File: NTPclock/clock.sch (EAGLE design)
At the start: 20 parts, among them IC1 MAX7219CNG

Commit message: Initial board layout
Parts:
- added R3: 10KΩ, SparkFun-Resistors:RESISTOR1206
- C6: device SparkFun-Capacitors:CAP_POLPTH4 -> SparkFun-Capacitors:CAP_POLPTH1
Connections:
- net +5V renamed VCC
- removed net +3.3V: C5.1, J1.2
- new net 3.3V: C5.1, J1.2, R3.1, U$1.3V3@0, U$1.3V3@1, U$1.3V3@2
- net SQL: now also R3.2
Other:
- moved on the sheet: C1, C2, C3, C4, C5, C6, C7, C8, DOUT, U$1

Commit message: Board update
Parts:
- C6: value (none) -> 470μF
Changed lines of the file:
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@@
 <part name="C4" library="SparkFun-Capacitors" deviceset="CAP" device="1206"/>
 <part name="C5" library="SparkFun-Capacitors" deviceset="CAP" device="1206"/>
-<part name="C6" library="SparkFun-Capacitors" deviceset="CAP_POL" device="PTH1"/>
+<part name="C6" library="SparkFun-Capacitors" deviceset="CAP_POL" device="PTH1" value="470μF"/>
 <part name="C7" library="SparkFun-Capacitors" deviceset="CAP_POL" device="PTH1"/>
 <part name="C8" library="SparkFun-Capacitors" deviceset="CAP_POL" device="PTH1" value="10μF"/>

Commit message: Update Schematic.  (Also break it)
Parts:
- U$1: value ESP12E_DEVKIT -> NODEMCU V3
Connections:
- net CLK: now also U$1.D7; no longer U$1.D6
- net DIGIT0: no longer DIG_3.G1, DIG_3.G2
- net DIGIT1: now also DIG_1.G1, DIG_1.G2; no longer DIG_2.G1, DIG_2.G2
- net DIGIT2: no longer DIG_1.G1, DIG_1.G2
- net DIGIT4: now also DIG_2.G1, DIG_2.G2
- net DIGIT5: now also DIG_3.G1, DIG_3.G2
- net LOAD: now also U$1.D6; no longer U$1.D7
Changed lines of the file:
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@@
 </classes>
 <parts>
-<part name="U$1" library="NODEMCUv1" deviceset="ESP12E_DEVKIT" device=""/>
+<part name="U$1" library="NODEMCUv1" deviceset="ESP12E_DEVKIT" device="" value="NODEMCU V3"/>
 <part name="IC1" library="max7219" deviceset="MAX7219CNG" device=""/>
 <part name="R1" library="SparkFun-Resistors" deviceset="RESISTOR" device="1206"/>
@@
 <net name="DIGIT0" class="0">
 <segment>
-<pinref part="DIG_3" gate="G$1" pin="G1"/>
-<pinref part="DIG_3" gate="G$1" pin="G2"/>
-<wire x1="76.2" y1="17.78" x2="76.2" y2="15.24" width="0.1524" layer="91"/>
-<wire x1="76.2" y1="10.16" x2="76.2" y2="15.24" width="0.1524" layer="91"/>
-<junction x="76.2" y="15.24"/>
-</segment>
-<segment>
 <pinref part="IC1" gate="G$1" pin="DIG0"/>
 <wire x1="58.42" y1="58.42" x2="55.88" y2="58.42" width="0.1524" layer="91"/>
@@
 <net name="DIGIT1" class="0">
 <segment>
-<pinref part="DIG_2" gate="G$1" pin="G1"/>
-<pinref part="DIG_2" gate="G$1" pin="G2"/>
-<wire x1="111.76" y1="17.78" x2="111.76" y2="15.24" width="0.1524" layer="91"/>
-<wire x1="111.76" y1="10.16" x2="111.76" y2="15.24" width="0.1524" layer="91"/>
-<junction x="111.76" y="15.24"/>
-</segment>
-<segment>
 <pinref part="IC1" gate="G$1" pin="DIG1"/>
 <wire x1="58.42" y1="55.88" x2="55.88" y2="55.88" width="0.1524" layer="91"/>
 </segment>
-</net>
-<net name="DIGIT2" class="0">
 <segment>
 <pinref part="DIG_1" gate="G$1" pin="G1"/>
@@
 <junction x="147.32" y="15.24"/>
 </segment>
+</net>
+<net name="DIGIT2" class="0">
 <segment>
 <pinref part="IC1" gate="G$1" pin="DIG2"/>
@@
 <junction x="236.22" y="15.24"/>
 </segment>
+<segment>
+<pinref part="DIG_3" gate="G$1" pin="G1"/>
+<pinref part="DIG_3" gate="G$1" pin="G2"/>
+<wire x1="76.2" y1="17.78" x2="76.2" y2="15.24" width="0.1524" layer="91"/>
+<wire x1="76.2" y1="10.16" x2="76.2" y2="15.24" width="0.1524" layer="91"/>
+<junction x="76.2" y="15.24"/>
+</segment>
 </net>
 <net name="DIGIT4" class="0">
@@
 <junction x="233.68" y="30.48"/>
 </segment>
+<segment>
+<pinref part="DIG_2" gate="G$1" pin="G1"/>
+<pinref part="DIG_2" gate="G$1" pin="G2"/>
+<wire x1="111.76" y1="17.78" x2="111.76" y2="15.24" width="0.1524" layer="91"/>
+</segment>
 </net>
 <net name="DATA" class="0">
@@
 <net name="CLK" class="0">
 <segment>
+<pinref part="IC1" gate="G$1" pin="CLK"/>
+<wire x1="27.94" y1="58.42" x2="20.32" y2="58.42" width="0.1524" layer="91"/>
+<label x="20.32" y="58.42" size="1.778" layer="95"/>
+</segment>
+<segment>
+<pinref part="U$1" gate="G$1" pin="D7"/>
+<wire x1="73.66" y1="101.6" x2="81.28" y2="101.6" width="0.1524" layer="91"/>
+<label x="76.2" y="101.6" size="1.778" layer="95"/>
+</segment>
+</net>
+<net name="LOAD" class="0">
+<segment>
+<pinref part="IC1" gate="G$1" pin="LOAD"/>
+<wire x1="27.94" y1="53.34" x2="20.32" y2="53.34" width="0.1524" layer="91"/>
+<label x="20.32" y="53.34" size="1.778" layer="95"/>
+</segment>
+<segment>
 <pinref part="U$1" gate="G$1" pin="D6"/>
 <wire x1="73.66" y1="104.14" x2="81.28" y2="104.14" width="0.1524" layer="91"/>
 <label x="76.2" y="104.14" size="1.778" layer="95"/>
 </segment>
-<segment>
-<pinref part="IC1" gate="G$1" pin="CLK"/>
-<wire x1="27.94" y1="58.42" x2="20.32" y2="58.42" width="0.1524" layer="91"/>
-<label x="20.32" y="58.42" size="1.778" layer="95"/>
-</segment>
-</net>
-<net name="LOAD" class="0">
-<segment>
-<pinref part="U$1" gate="G$1" pin="D7"/>
-<wire x1="73.66" y1="101.6" x2="81.28" y2="101.6" width="0.1524" layer="91"/>
-<label x="76.2" y="101.6" size="1.778" layer="95"/>
-</segment>
-<segment>
-<pinref part="IC1" gate="G$1" pin="LOAD"/>
-<wire x1="27.94" y1="53.34" x2="20.32" y2="53.34" width="0.1524" layer="91"/>
-<label x="20.32" y="53.34" size="1.778" layer="95"/>
-</segment>
-</net>
+</net>

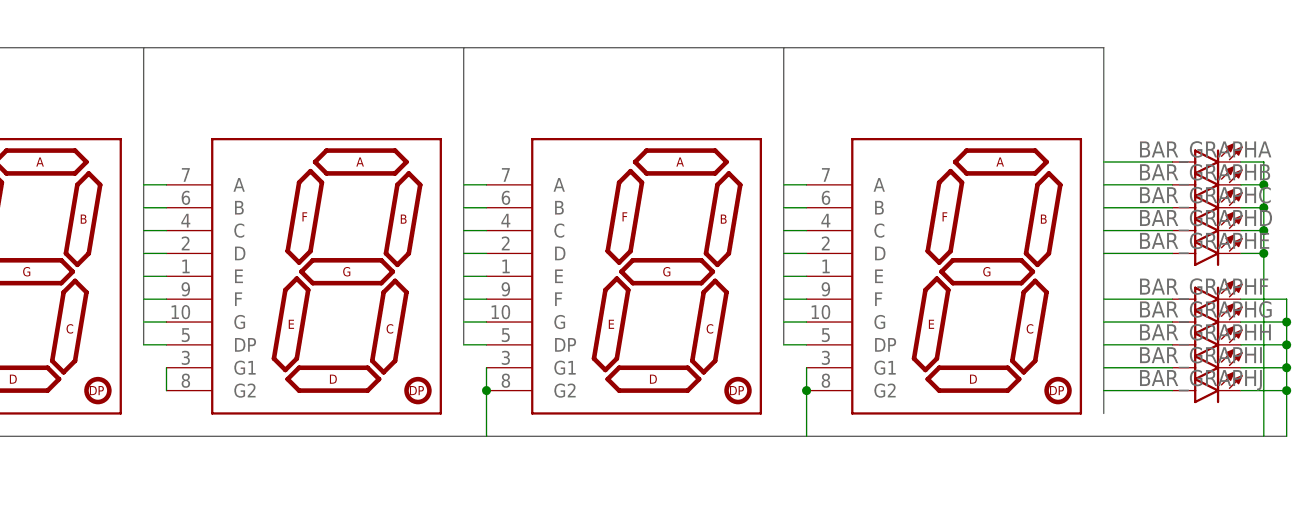
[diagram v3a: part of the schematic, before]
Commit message: rearange digits
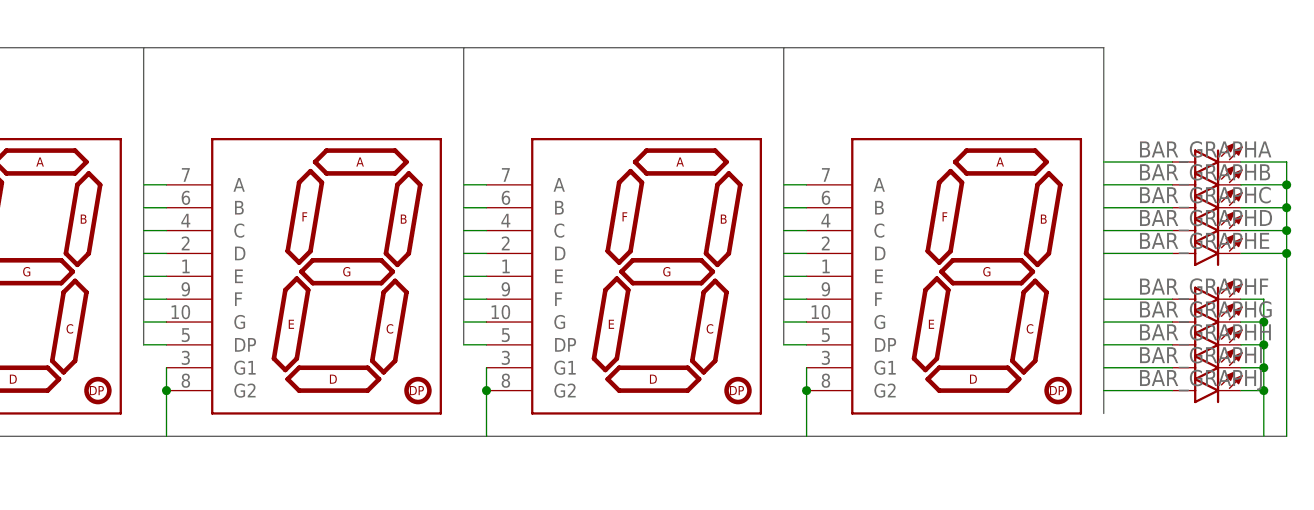
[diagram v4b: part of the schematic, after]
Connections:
- net DIGIT1: now also DIG_2.G1, DIG_2.G2; no longer DIG_1.G1, DIG_1.G2
- net DIGIT3: now also BAR_GRAPHA.C, BAR_GRAPHB.C, BAR_GRAPHC.C, BAR_GRAPHD.C, BAR_GRAPHE.C; no longer DIG_0.G1, DIG_0.G2
- net DIGIT4: now also DIG_1.G1, DIG_1.G2; no longer BAR_GRAPHA.C, BAR_GRAPHB.C, BAR_GRAPHC.C, BAR_GRAPHD.C, BAR_GRAPHE.C, DIG_2.G1, DIG_2.G2
- net DIGIT5: no longer BAR_GRAPHF.C, BAR_GRAPHG.C, BAR_GRAPHH.C, BAR_GRAPHI.C, BAR_GRAPHJ.C
- net DIGIT6: now also DIG_0.G1, DIG_0.G2
- net DIGIT7: now also BAR_GRAPHF.C, BAR_GRAPHG.C, BAR_GRAPHH.C, BAR_GRAPHI.C, BAR_GRAPHJ.C

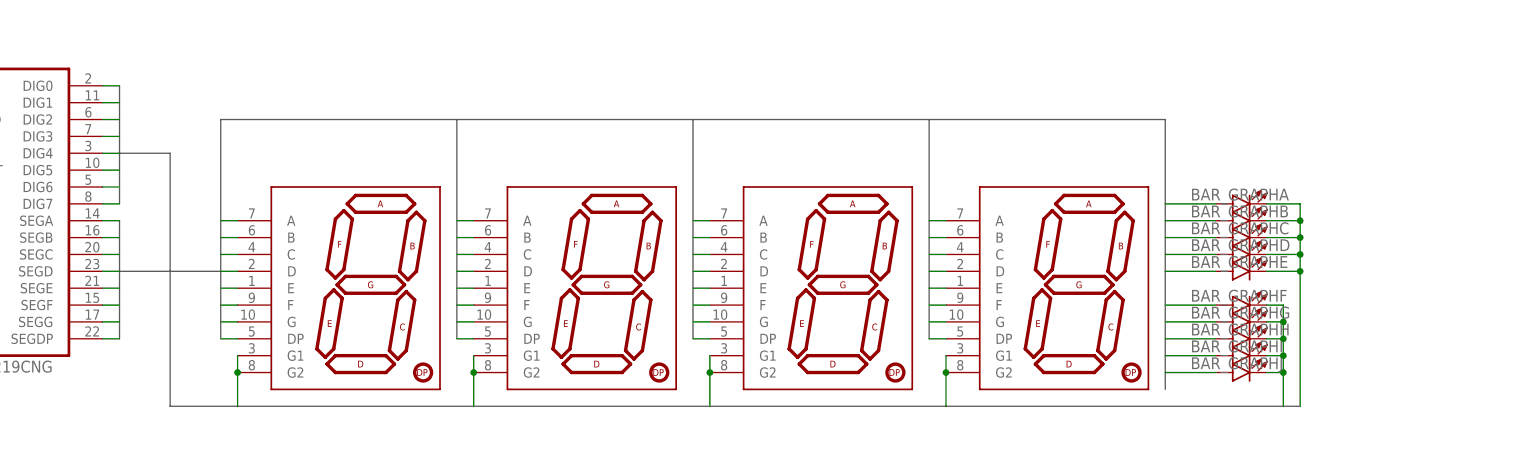
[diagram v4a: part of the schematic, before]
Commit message: Add Ground pour(s)
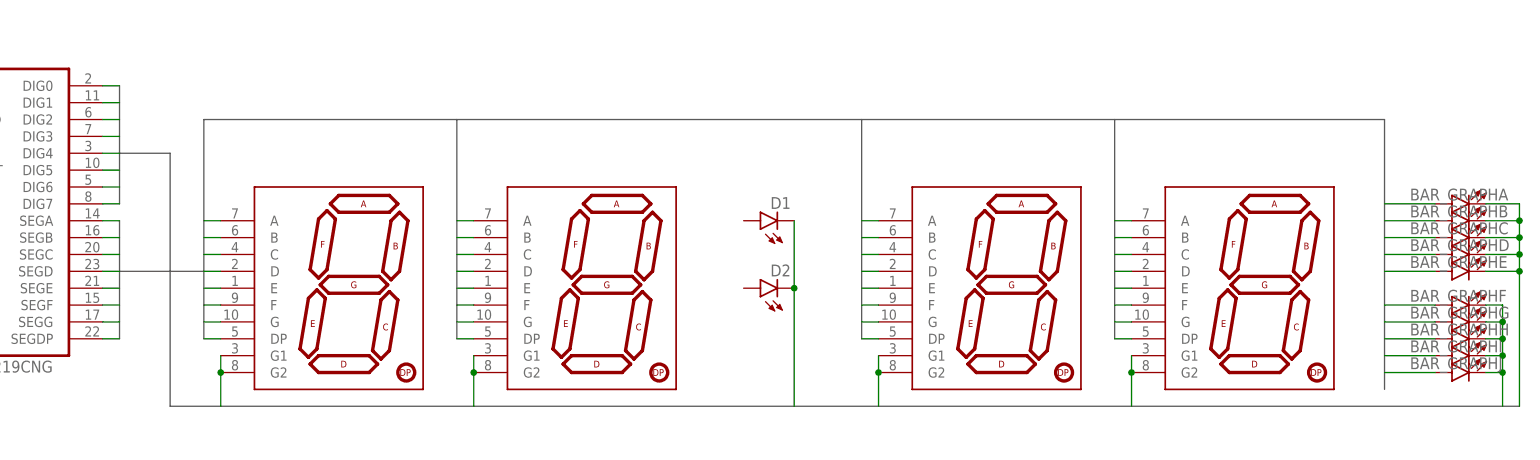
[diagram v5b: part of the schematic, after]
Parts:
- added D1, D2: (no value), SparkFun-LED:LED3MM
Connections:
- net DIGIT0: now also DIG_1.G1, DIG_1.G2
- net DIGIT4: now also D1.C, D2.C; no longer DIG_1.G1, DIG_1.G2
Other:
- moved on the sheet: BAR_GRAPHA, BAR_GRAPHB, BAR_GRAPHC, BAR_GRAPHD, BAR_GRAPHE, BAR_GRAPHF, BAR_GRAPHG, BAR_GRAPHH, BAR_GRAPHI, BAR_GRAPHJ
